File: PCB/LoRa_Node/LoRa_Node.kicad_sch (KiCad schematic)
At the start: 75 parts, among them IC1 SPX5205M5-L/TR, J1 Conn_01x04_Socket, J2 Conn_01x02_Pin, J3 UF.L, J4 2x5_2.00mm, J6 Conn_01x06_Socket, J7 Conn_01x03_Socket, Q1 AO3401A, SW1 SW_SPST, U1 BME280, U2 RFM95W-868S2, U3 STM32L151C8T6, U4 SIM800L-CORE, U5 SX1308, Y1 12MHz, Y2 32.768kHz

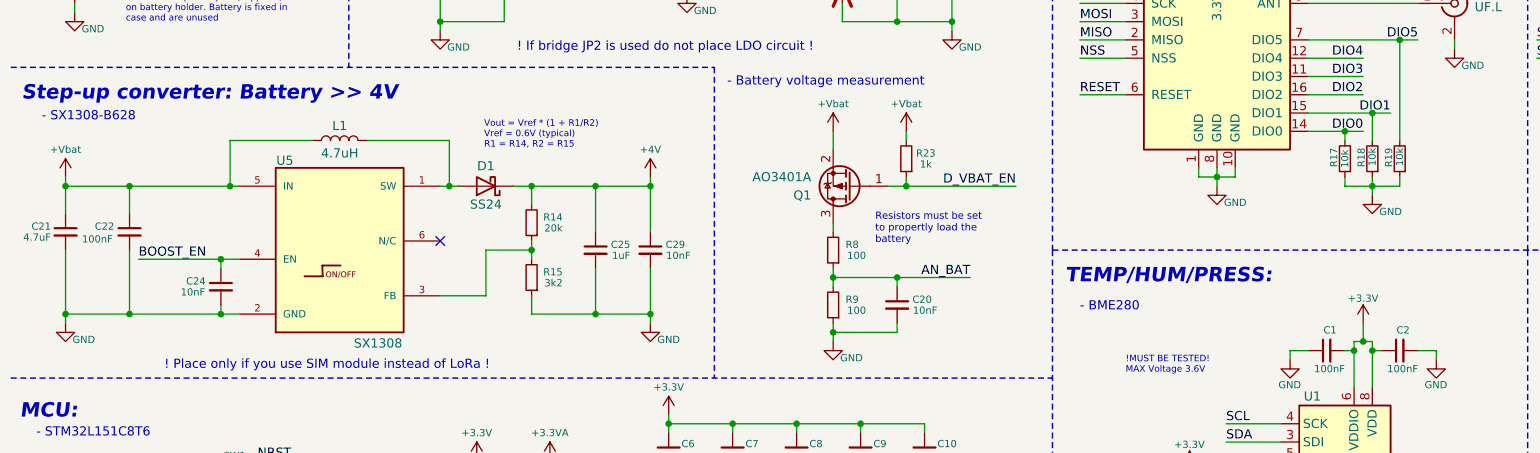
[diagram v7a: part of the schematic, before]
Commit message: Update
firmware current optimisation
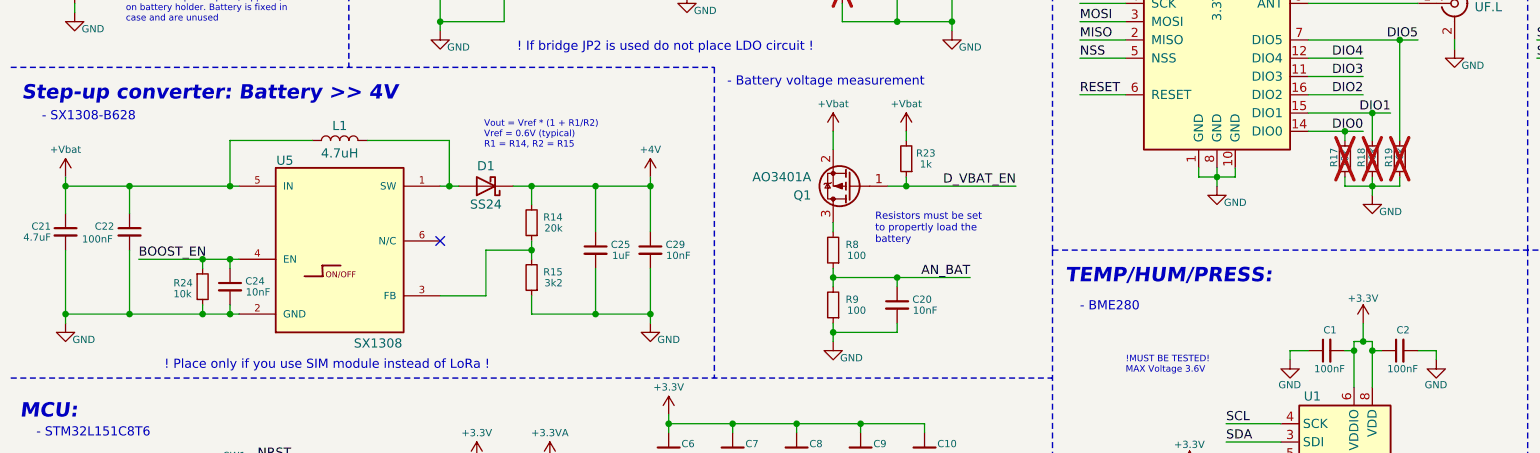
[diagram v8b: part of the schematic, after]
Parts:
- added R24: 10k, Resistor_SMD:R_0603_1608Metric, symbol Device:R_Small
- R17, R18, R19: now not fitted
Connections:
- net BOOST_EN: now also R24.1
- net GND: now also R24.2
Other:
- moved on the sheet: C24
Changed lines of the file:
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@@
 	)
 	(junction
-		(at 41.91 87.63)
-		(diameter 0)
-		(color 0 0 0 0)
-	)
-	(junction
 		(at 29.21 69.85)
 		(diameter 0)
@@
 	)
 	(junction
+		(at 43.18 80.01)
+		(diameter 0)
+		(color 0 0 0 0)
+	)
+	(junction
 		(at 43.18 69.85)
 		(diameter 0)
@@
 	)
 	(junction
+		(at 39.37 80.01)
+		(diameter 0)
+		(color 0 0 0 0)
+	)
+	(junction
 		(at 176.53 110.49)
 		(diameter 0)
@@
 	)
 	(junction
+		(at 39.37 87.63)
+		(diameter 0)
+		(color 0 0 0 0)
+	)
+	(junction
 		(at 55.88 110.49)
 		(diameter 0)
@@
 	)
 	(junction
+		(at 43.18 87.63)
+		(diameter 0)
+		(color 0 0 0 0)
+	)
+	(junction
 		(at 143.51 29.21)
 		(diameter 0)
@@
 	)
 	(junction
-		(at 41.91 80.01)
-		(diameter 0)
-		(color 0 0 0 0)
-	)
-	(junction
 		(at 113.03 110.49)
 		(diameter 0)
@@
 	(wire
 		(pts
-			(xy 41.91 80.01) (xy 41.91 81.28)
+			(xy 43.18 80.01) (xy 43.18 81.28)
 		)
 		(stroke
@@
 		)
 	)
+	(wire
+		(pts
+			(xy 39.37 80.01) (xy 39.37 81.28)
+		)
+		(stroke
+			(width 0)
+			(type default)
+		)
+	)
 	(polyline
 		(pts
@@
 	(wire
 		(pts
-			(xy 41.91 87.63) (xy 44.45 87.63)
-		)
-		(stroke
-			(width 0)
-			(type default)
-		)
-	)
-	(wire
-		(pts
 			(xy 85.09 69.85) (xy 93.98 69.85)
 		)
@@
 	(wire
 		(pts
-			(xy 30.48 80.01) (xy 41.91 80.01)
+			(xy 30.48 80.01) (xy 39.37 80.01)
+		)
+		(stroke
+			(width 0)
+			(type default)
+		)
+	)
+	(wire
+		(pts
+			(xy 39.37 87.63) (xy 43.18 87.63)
 		)
 		(stroke
@@
 	(wire
 		(pts
+			(xy 43.18 80.01) (xy 44.45 80.01)
+		)
+		(stroke
+			(width 0)
+			(type default)
+		)
+	)
+	(wire
+		(pts
 			(xy 20.32 73.66) (xy 20.32 69.85)
 		)
@@
 	(wire
 		(pts
-			(xy 41.91 86.36) (xy 41.91 87.63)
+			(xy 43.18 86.36) (xy 43.18 87.63)
 		)
 		(stroke
@@
 	(wire
 		(pts
-			(xy 29.21 87.63) (xy 41.91 87.63)
+			(xy 29.21 87.63) (xy 39.37 87.63)
 		)
 		(stroke
@@
 	(wire
 		(pts
+			(xy 39.37 80.01) (xy 43.18 80.01)
+		)
+		(stroke
+			(width 0)
+			(type default)
+		)
+	)
+	(wire
+		(pts
 			(xy 46.99 152.4) (xy 46.99 153.67)
 		)
@@
 		)
 	)
-	(wire
-		(pts
-			(xy 41.91 80.01) (xy 44.45 80.01)
-		)
-		(stroke
-			(width 0)
-			(type default)
-		)
-	)
 	(polyline
 		(pts
@@
 	(wire
 		(pts
+			(xy 43.18 87.63) (xy 44.45 87.63)
+		)
+		(stroke
+			(width 0)
+			(type default)
+		)
+	)
+	(wire
+		(pts
 			(xy 137.16 69.85) (xy 152.4 69.85)
 		)
@@
 	(wire
 		(pts
+			(xy 39.37 86.36) (xy 39.37 87.63)
+		)
+		(stroke
+			(width 0)
+			(type default)
+		)
+	)
+	(wire
+		(pts
 			(xy 139.7 120.65) (xy 139.7 119.38)
 		)
@@
 		(in_bom yes)
 		(on_board yes)
-		(dnp no)
+		(dnp yes)
 		(property "Reference" "R17"
 			(at 196.596 64.516 90)
@@
 		(in_bom yes)
 		(on_board yes)
-		(dnp no)
+		(dnp yes)
 		(property "Reference" "R19"
 			(at 204.216 64.516 90)
@@
 	(symbol
 		(lib_id "Device:C_Small")
-		(at 41.91 83.82 0)
+		(at 43.18 83.82 0)
+		(mirror y)
 		(unit 1)
 		(exclude_from_sim no)
@@
 		(dnp no)
 		(property "Reference" "C24"
-			(at 37.084 83.058 0)
+			(at 48.006 83.058 0)
 			(effects
 				(font
@@
 		)
 		(property "Value" "10nF"
-			(at 36.322 84.582 0)
+			(at 48.768 84.582 0)
 			(effects
 				(font
@@
 		)
 		(property "Footprint" "Capacitor_SMD:C_0603_1608Metric"
-			(at 41.91 83.82 0)
+			(at 43.18 83.82 0)
 			(effects
 				(font
@@
 		)
 		(property "Datasheet" "~"
-			(at 41.91 83.82 0)
+			(at 43.18 83.82 0)
 			(effects
 				(font
@@
 		)
 		(property "Description" ""
-			(at 41.91 83.82 0)
+			(at 43.18 83.82 0)
 			(effects
 				(font
@@
 		(in_bom yes)
 		(on_board yes)
-		(dnp no)
+		(dnp yes)
 		(property "Reference" "R18"
 			(at 200.406 64.516 90)
@@
 					(unit 1)
 				)
+			)
+		)
+	)
+	(symbol
+		(lib_id "Device:R_Small")
+		(at 39.37 83.82 0)
+		(unit 1)
+		(exclude_from_sim no)
+		(in_bom yes)
+		(on_board yes)
+		(dnp no)
+		(property "Reference" "R24"
+			(at 35.306 83.312 0)
+			(effects
+				(font
+					(size 1 1)
+				)
+				(justify left)
+			)
+		)
+		(property "Value" "10k"
+			(at 35.306 84.836 0)
+			(effects
+				(font
+					(size 1 1)
+				)
+				(justify left)
+			)
+		)
+		(property "Footprint" "Resistor_SMD:R_0603_1608Metric"
+			(at 39.37 83.82 0)
+			(effects
+				(font
+					(size 1.27 1.27)
+				)
+				(hide yes)
+			)
+		)
+		(property "Datasheet" "~"
+			(at 39.37 83.82 0)
+			(effects
+				(font
+					(size 1.27 1.27)
+				)
+				(hide yes)
+			)
+		)
+		(property "Description" ""
+			(at 39.37 83.82 0)
+			(effects
+				(font
+					(size 1.27 1.27)
+				)
+				(hide yes)
+			)
+		)
+		(pin "1"
+		)
+		(pin "2"
+		)
+		(instances
+			(project "LoRa_Node"
+				(path "/5b3a9ed5-b573-4749-b018-914b5f316832"
+					(reference "R24")
+					(unit 1)
+				)
